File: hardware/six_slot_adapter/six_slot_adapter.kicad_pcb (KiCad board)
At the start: 2 copper layers, 100 x 100 mm, 22 parts, among them J3 CART SLOT TOP ROW, J4 CART SLOT BOTTOM ROW, M2_1 Screw_Terminal_01x01, M2_2 Screw_Terminal_01x01, M2_3 Screw_Terminal_01x01, M2_4 Screw_Terminal_01x01, M2_5 Screw_Terminal_01x01, M2_6 Screw_Terminal_01x01, M2_7 Screw_Terminal_01x01, M2_8 Screw_Terminal_01x01, M2_9 Screw_Terminal_01x01

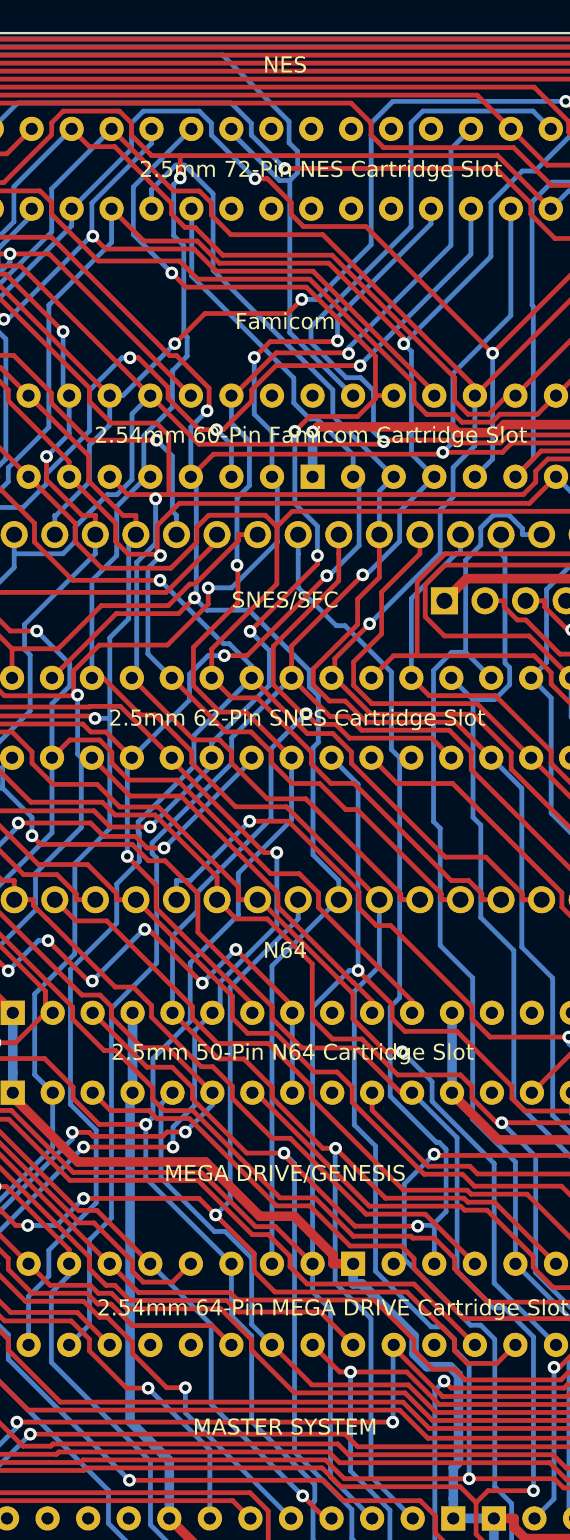
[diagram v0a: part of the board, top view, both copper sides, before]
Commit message: six-slot adapter: update labels; -> kicad v7
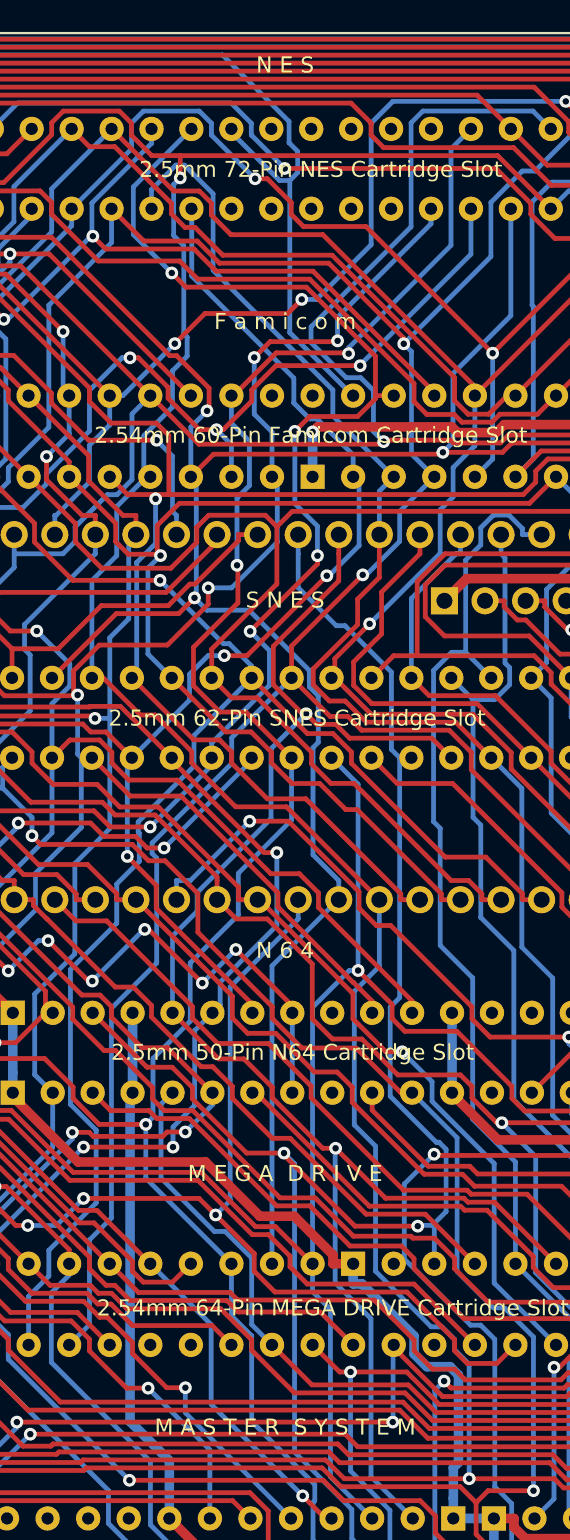
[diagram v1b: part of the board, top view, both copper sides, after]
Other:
- board text added: "F a m i c o m"
- board text added: "M A S T E R S Y S T E M"
- board text added: "M E G A D R I V E"
- board text added: "N 6 4"
- board text added: "N E S"
- board text added: "S N E S"
- board text removed: "Famicom"
- board text removed: "MASTER SYSTEM"
- board text removed: "MEGA DRIVE/GENESIS"
- board text removed: "N64"
- board text removed: "NES"
- board text removed: "SNES/SFC"
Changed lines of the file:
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@@
       (plot_on_all_layers_selection 0x0000000_00000000)
       (disableapertmacros false)
-      (usegerberextensions false)
-      (usegerberattributes true)
-      (usegerberadvancedattributes true)
-      (creategerberjobfile true)
+      (usegerberextensions true)
+      (usegerberattributes false)
+      (usegerberadvancedattributes false)
+      (creategerberjobfile false)
       (dashed_line_dash_ratio 12.000000)
       (dashed_line_gap_ratio 3.000000)
@@
       (plotinvisibletext false)
       (sketchpadsonfab false)
-      (subtractmaskfromsilk false)
+      (subtractmaskfromsilk true)
       (outputformat 1)
       (mirror false)
@@
     (effects (font (size 0.7 0.7) (thickness 0.15)) (justify mirror))
   )
-  (gr_text "NES" (at 150 52) (layer "F.SilkS" knockout)
+  (gr_text "N E S" (at 150 52) (layer "F.SilkS" knockout)
     (effects (font (size 1 1) (thickness 0.15)))
   )
@@
     (effects (font (size 1 1) (thickness 0.15)))
   )
-  (gr_text "Famicom" (at 150 68.06) (layer "F.SilkS" knockout)
+  (gr_text "F a m i c o m" (at 150 68.06) (layer "F.SilkS" knockout)
     (effects (font (size 1 1) (thickness 0.15)))
   )
-  (gr_text "SNES/SFC" (at 150 85.5) (layer "F.SilkS" knockout)
+  (gr_text "S N E S" (at 150 85.5) (layer "F.SilkS" knockout)
     (effects (font (size 1 1) (thickness 0.15)))
   )
@@
     (effects (font (size 1 1) (thickness 0.15)))
   )
-  (gr_text "MEGA DRIVE/GENESIS" (at 150 121.4) (layer "F.SilkS" knockout)
+  (gr_text "M E G A  D R I V E" (at 150 121.4) (layer "F.SilkS" knockout)
     (effects (font (size 1 1) (thickness 0.15)))
   )
-  (gr_text "N64" (at 150 107.43) (layer "F.SilkS" knockout)
+  (gr_text "N 6 4" (at 150 107.43) (layer "F.SilkS" knockout)
     (effects (font (size 1 1) (thickness 0.15)))
   )
@@
     (effects (font (size 1 1) (thickness 0.15)))
   )
-  (gr_text "MASTER SYSTEM" (at 150 137.275) (layer "F.SilkS" knockout)
+  (gr_text "M A S T E R  S Y S T E M" (at 150 137.275) (layer "F.SilkS" knockout)
     (effects (font (size 1 1) (thickness 0.15)))
   )
